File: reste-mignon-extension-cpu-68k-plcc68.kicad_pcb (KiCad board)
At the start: 2 copper layers, 99.1 x 99.1 mm, 20 parts, among them J1 RESTE_MIGNON_CPU_CONNECTOR_A, J2 RESTE_MIGNON_CPU_CONNECTOR_B, U1 MC68000_PLCC_68_PHY

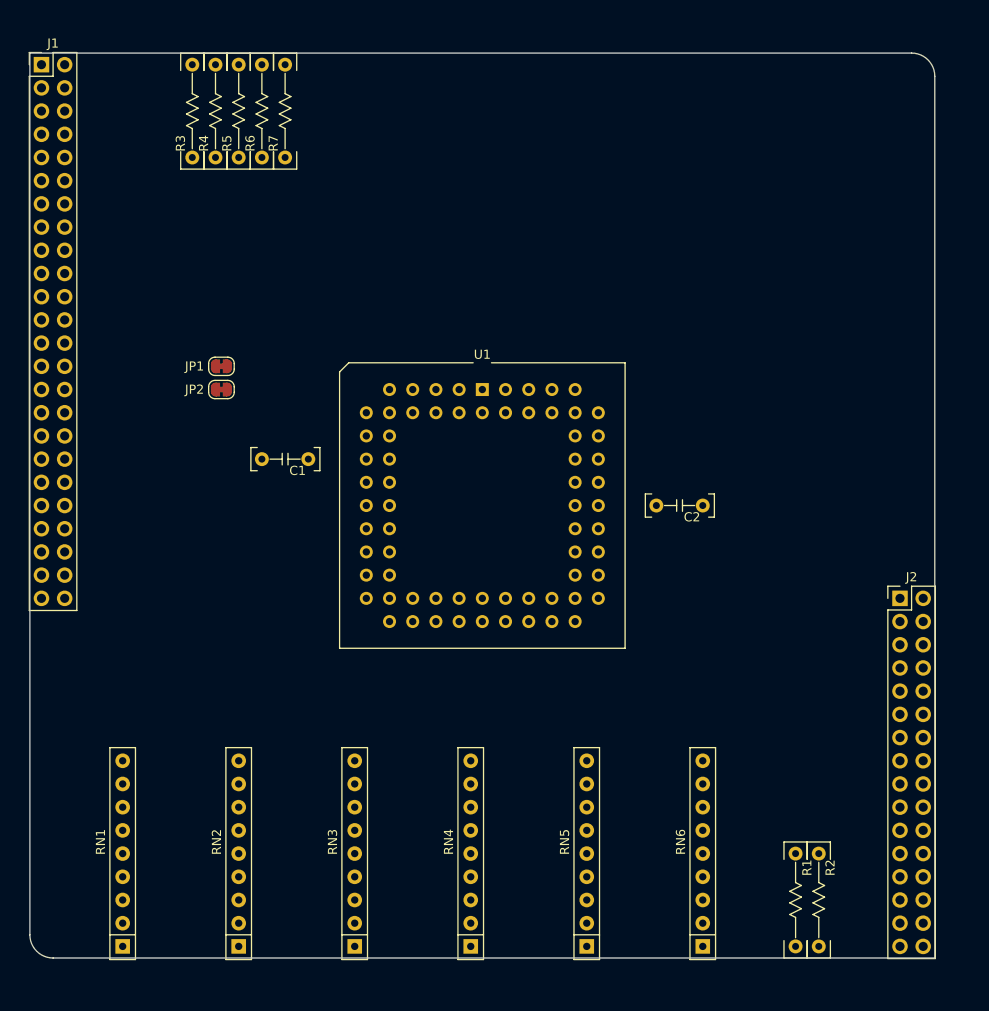
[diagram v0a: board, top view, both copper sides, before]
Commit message: pcb session -- change cpu orientation for easier routing
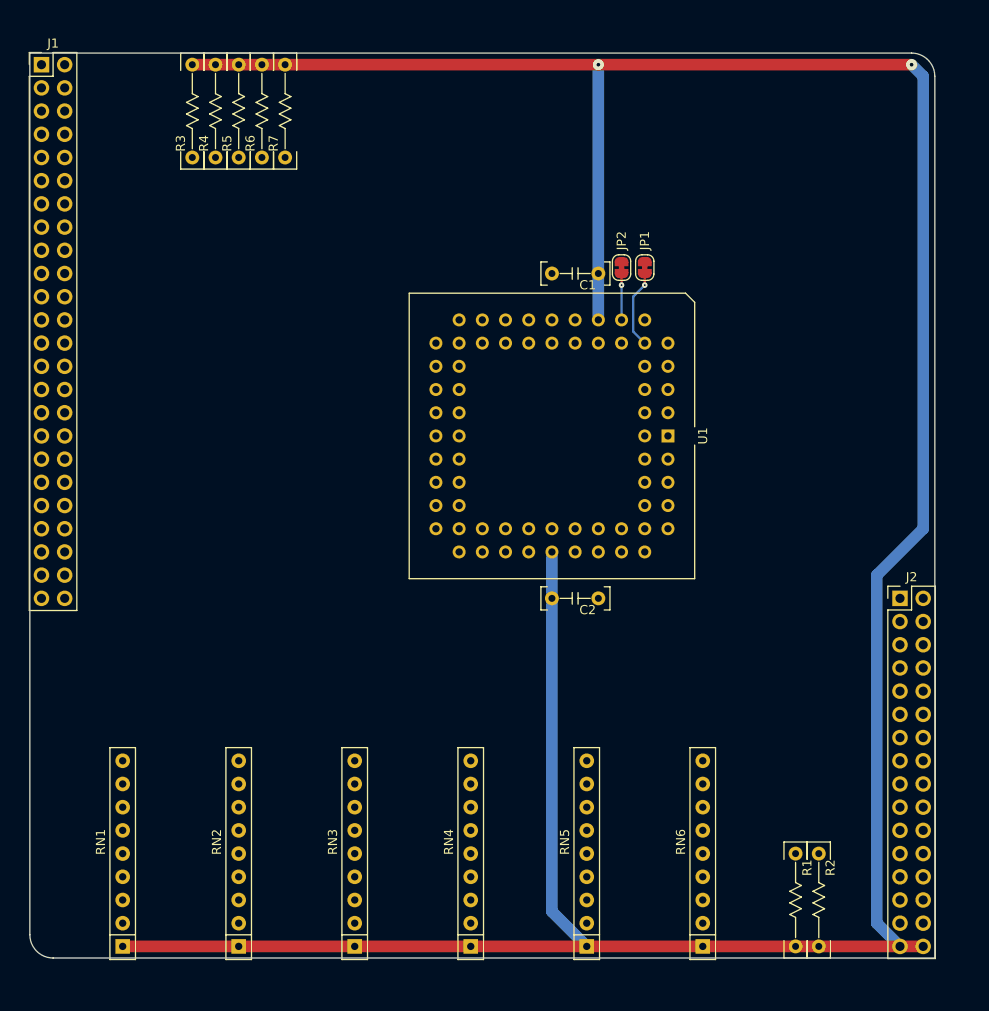
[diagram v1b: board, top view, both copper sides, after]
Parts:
- moved JP1 47.6 mm to (120.7, 125.1), turned to -90 degrees
- moved JP2 45.8 mm to (118.1, 125.1), turned to -90 degrees
- moved C1 37.7 mm to (113.0, 125.7)
- moved U1 20.9 mm to (123.2, 143.5), turned to -90 degrees
- moved C2 15.3 mm to (113.0, 161.3)
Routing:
- net /VCC: track 0.00 -> 339.3 mm, vias 0 -> 2
- net /~{BG}: track 0.00 -> 8.67 mm, vias 0 -> 1
- net /~{BGACK}: track 0.00 -> 5.08 mm, vias 0 -> 1

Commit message: pcb session -- start wiring
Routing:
- net /~{BLT.BG}: track 0.00 -> 79.2 mm, vias 0 -> 2
- net /~{BLT.BGACK}: track 0.00 -> 74.9 mm, vias 0 -> 2
- net /~{VMA}: track 0.00 -> 29.2 mm, vias 0 -> 1
- net /FC0: track 0.00 -> 29.2 mm, vias 0 -> 1
- net /~{VPA}: track 0.00 -> 28.5 mm, vias 0 -> 1
- net /FC1: track 0.00 -> 28.5 mm, vias 0 -> 1
- net /FC2: track 0.00 -> 23.4 mm, vias 0 -> 1
- net /~{DTACK}: track 0.00 -> 16.5 mm, vias 0 -> 1
- net /~{RESET}: track 0.00 -> 11.4 mm, vias 0 -> 1
- net /~{AS}: track 0.00 -> 8.15 mm
- net /R/~{W}: track 0.00 -> 8.15 mm
- net /D8: track 0.00 -> 8.15 mm
- net /D5: track 0.00 -> 8.15 mm
- net /D3: track 0.00 -> 8.15 mm
- net /D15: track 0.00 -> 8.15 mm
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
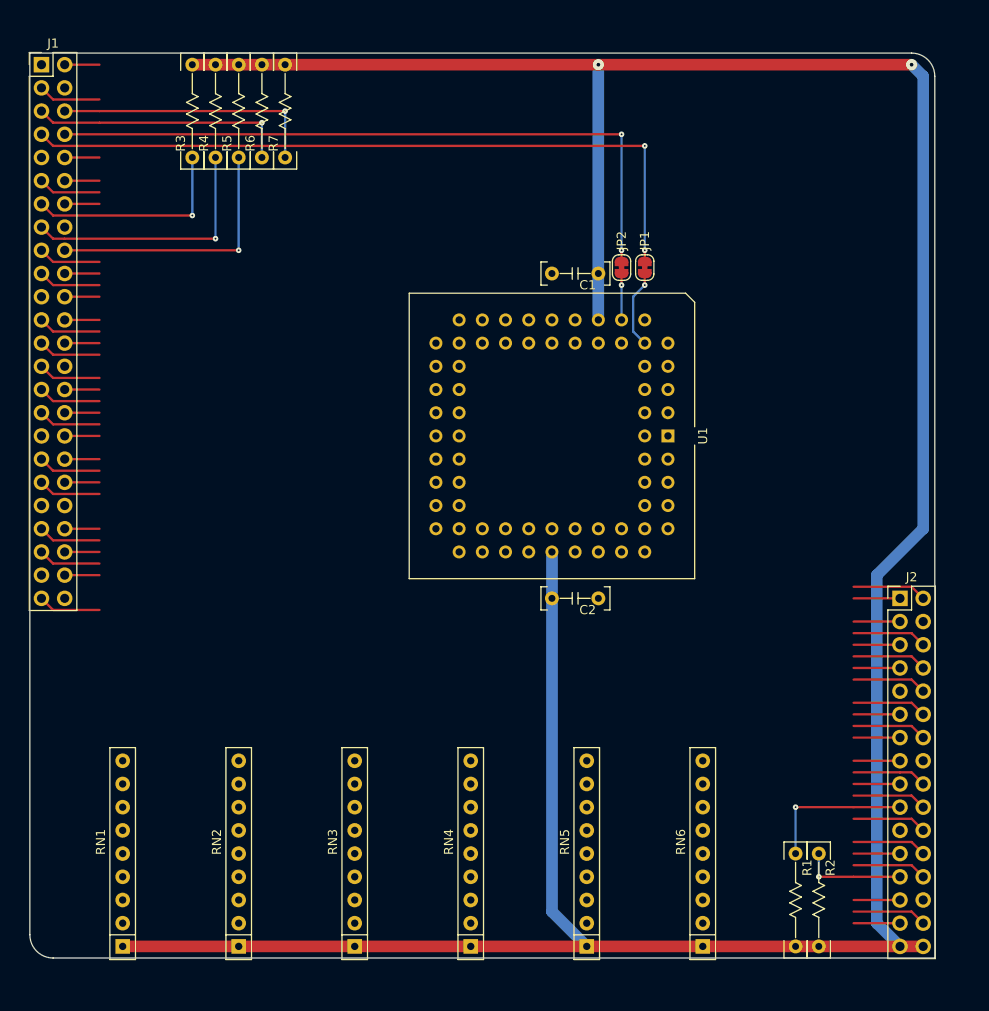
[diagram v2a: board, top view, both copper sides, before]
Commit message: pcb session -- start pull-ups, adjust pull-up mapping of RN1 for ease of routing
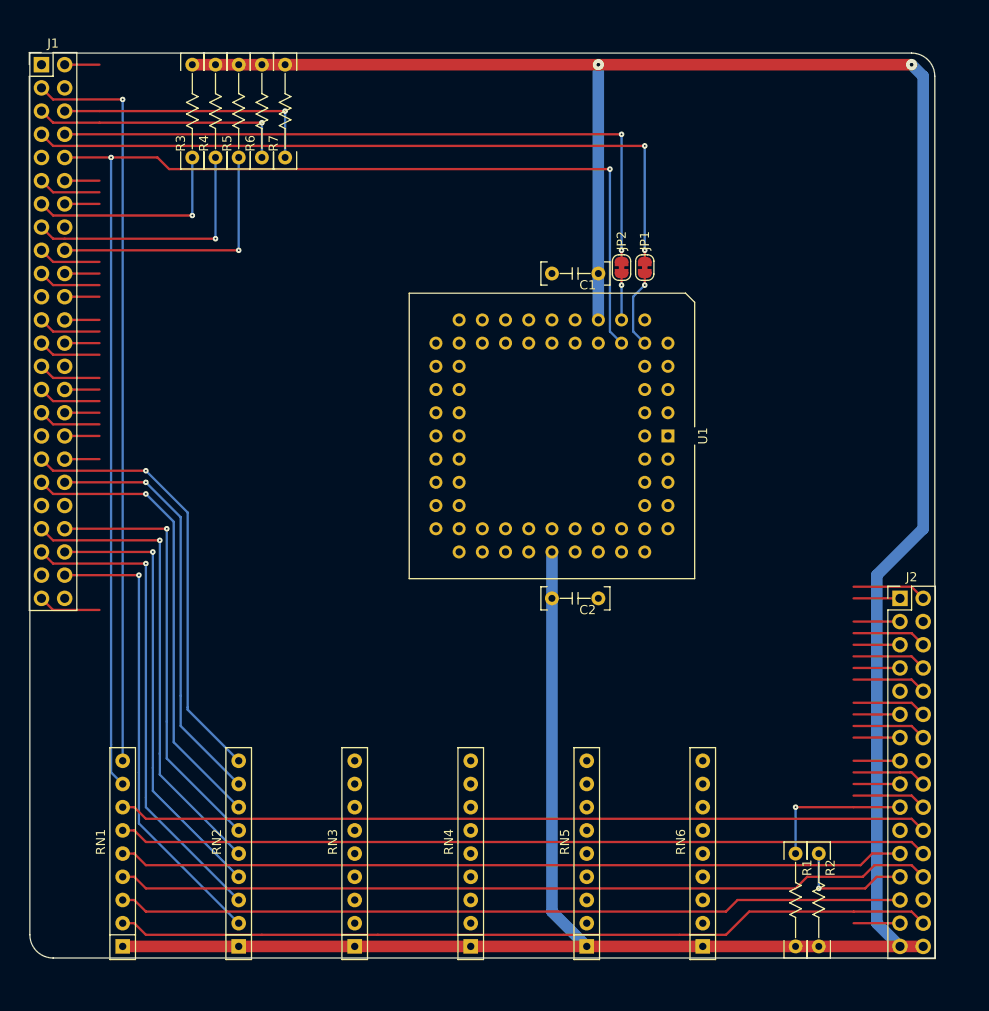
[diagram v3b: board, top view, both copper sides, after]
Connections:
- RN1 pad 2: /~{HALT} -> /~{BGACK}
- RN1 pad 3: /~{BERR} -> /~{HALT}
- RN1 pad 4: /~{BGACK} -> /~{AS}
- RN1 pad 5: /~{BR} -> /~{UDS}
- RN1 pad 6: /R/~{W} -> /~{LDS}
- RN1 pad 7: /~{LDS} -> /R/~{W}
- RN1 pad 8: /~{UDS} -> /~{BR}
- RN1 pad 9: /~{AS} -> /~{BERR}
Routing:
- net /~{BR}: track 3.81 -> 148.9 mm, vias 0 -> 2
- net /~{AS}: track 8.15 -> 89.7 mm
- net /~{BGACK}: track 13.2 -> 94.8 mm
- net /~{UDS}: track 5.08 -> 86.1 mm
- net /~{HALT}: track 5.08 -> 86.1 mm
- net /~{LDS}: track 8.15 -> 88.7 mm
- net /R/~{W}: track 8.15 -> 88.7 mm
- net /~{BERR}: track 6.88 -> 81.8 mm, vias 0 -> 1
- net /A1: track 3.81 -> 50.8 mm, vias 0 -> 1
- net /A2: track 6.88 -> 53.0 mm, vias 0 -> 1
- net /A3: track 3.81 -> 49.1 mm, vias 0 -> 1
- net /A4: track 6.88 -> 51.3 mm, vias 0 -> 1
- net /A5: track 3.81 -> 47.5 mm, vias 0 -> 1
- net /A6: track 6.88 -> 50.5 mm, vias 0 -> 1
- net /A7: track 3.81 -> 46.1 mm, vias 0 -> 1
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
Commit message: pcb session -- continue pull-ups, done a1-a12
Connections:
- RN4 pad 2: /A17 -> /A23
- RN4 pad 3: /A18 -> /A22
- RN4 pad 4: /A19 -> /A21
- RN4 pad 6: /A21 -> /A19
- RN4 pad 7: /A22 -> /A18
- RN4 pad 8: /A23 -> /A17
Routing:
- net /A9: track 3.81 -> 103.8 mm, vias 0 -> 4
- net /A10: track 3.81 -> 97.8 mm, vias 0 -> 4
- net /A11: track 6.88 -> 99.2 mm, vias 0 -> 2
- net /A12: track 3.81 -> 91.2 mm, vias 0 -> 2
- net /A14: track 3.81 -> 67.7 mm, vias 0 -> 1
- net /A16: track 6.88 -> 69.5 mm, vias 0 -> 1
- net /A13: track 6.88 -> 68.9 mm, vias 0 -> 1
- net /A23: track 6.88 -> 68.3 mm, vias 0 -> 2
- net /A15: track 6.88 -> 66.4 mm, vias 0 -> 1
- net /A1: track 50.8 -> 105.4 mm, vias 1 -> 3
- net /A22: track 3.81 -> 57.3 mm, vias 0 -> 2
- net /A21: track 6.88 -> 58.5 mm, vias 0 -> 2
- net /A3: track 49.1 -> 98.6 mm, vias 1 -> 3
- net /A2: track 53.0 -> 102.0 mm, vias 1 -> 3
- net /A5: track 47.5 -> 91.8 mm, vias 1 -> 3
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
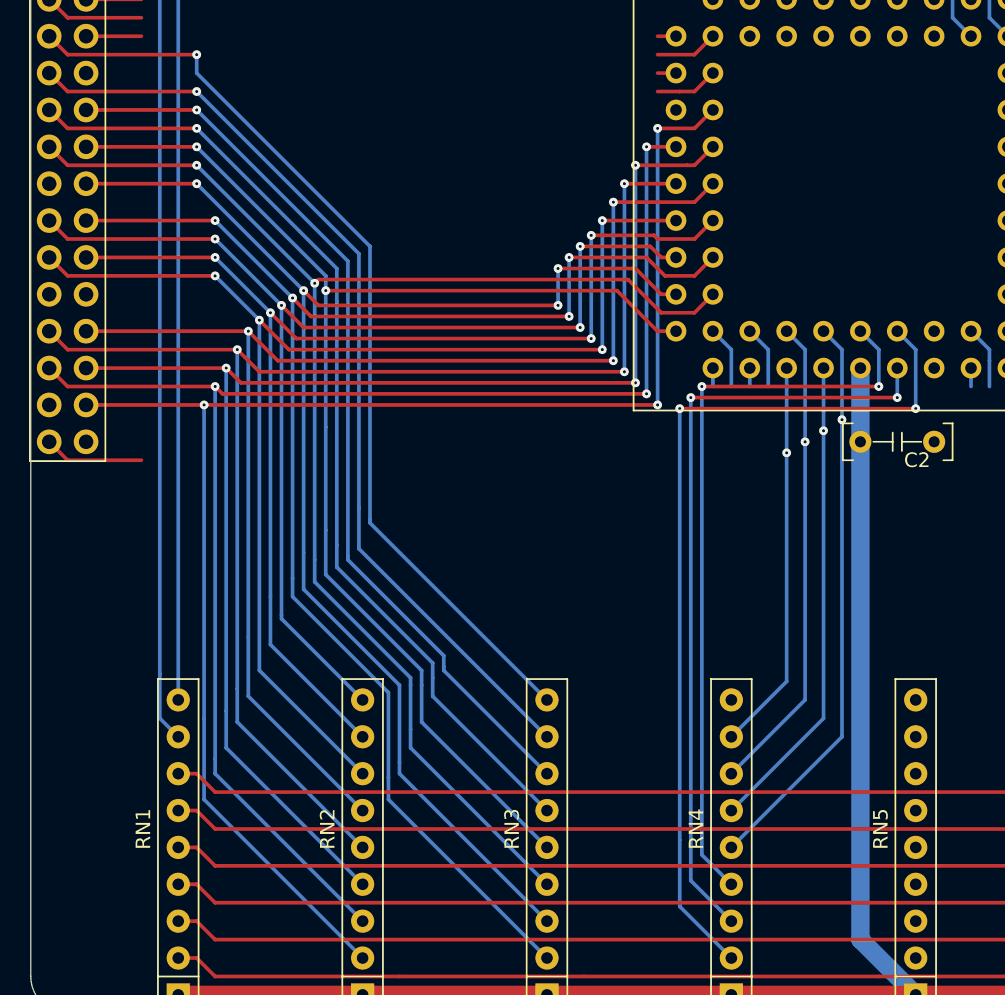
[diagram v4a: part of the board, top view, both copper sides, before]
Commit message: pcb session -- switch to 4 layers, spread vias to avoid cuts in ground plane
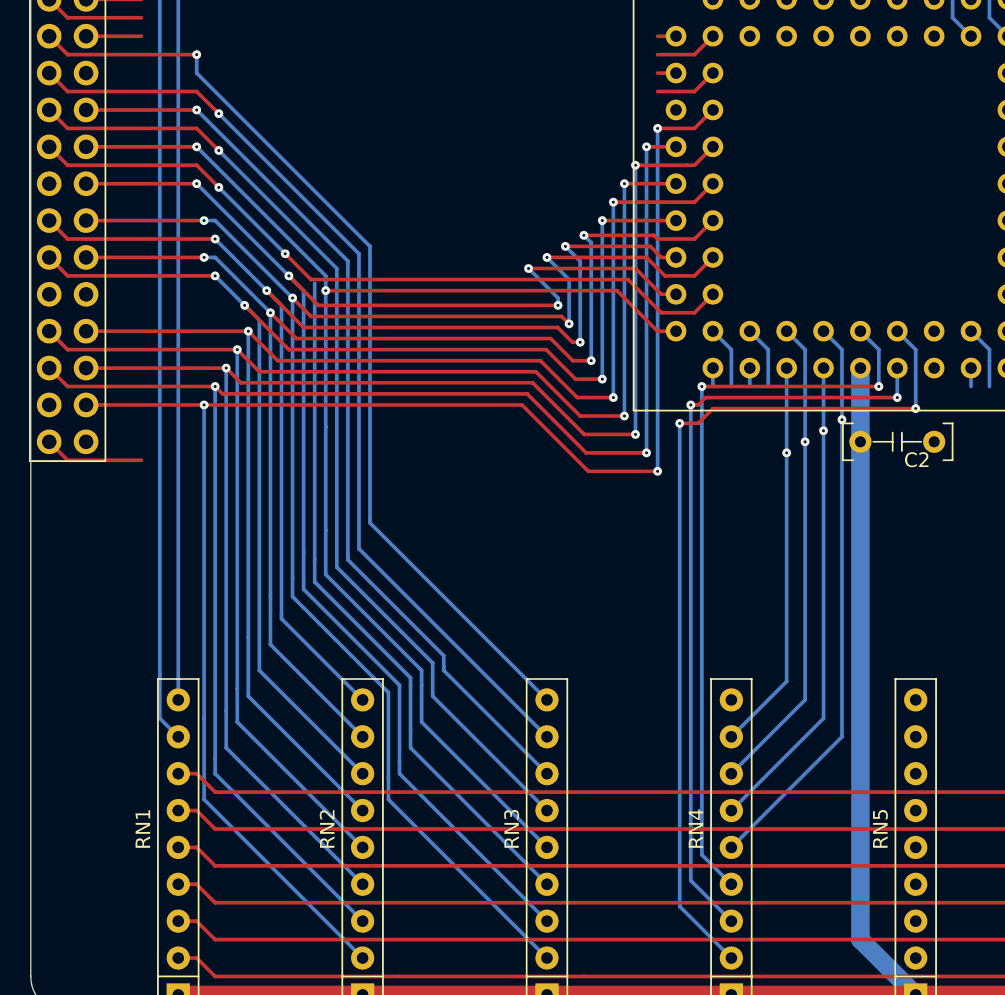
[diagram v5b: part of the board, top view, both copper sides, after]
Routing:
- net /A1: track 105.4 -> 111.8 mm
- net /A2: track 102.0 -> 107.7 mm
- net /A3: track 98.6 -> 103.6 mm
- net /A6: track 88.9 -> 93.2 mm
- net /A4: track 95.2 -> 99.5 mm
- net /A10: track 97.8 -> 102.1 mm
- net /A8: track 81.6 -> 85.9 mm
- net /A5: track 91.8 -> 95.3 mm
- net /A9: track 103.8 -> 106.6 mm
- net /A7: track 85.1 -> 88.0 mm
- net /A23: track 68.3 -> 67.7 mm
- added copper zone on In1.Cu, net /GND
- added copper zone on In2.Cu, net /GND
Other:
- copper layers 2 -> 4

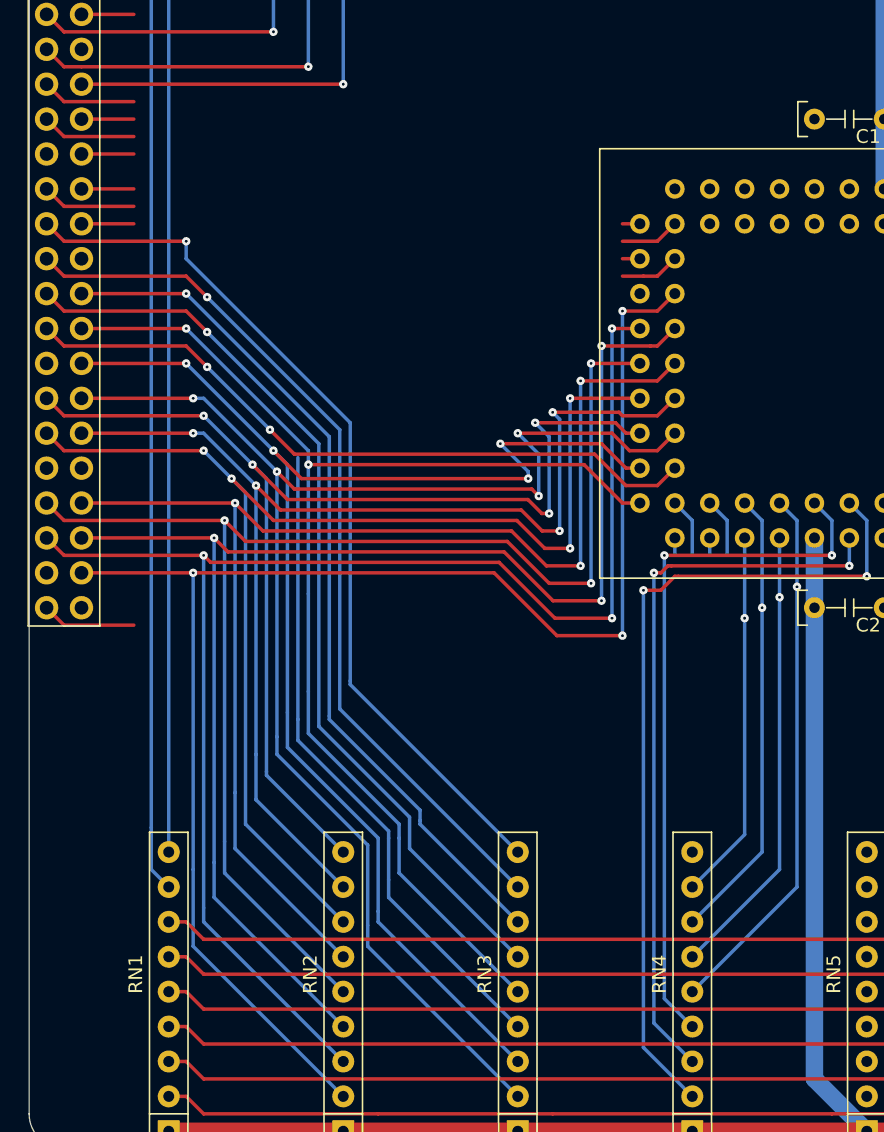
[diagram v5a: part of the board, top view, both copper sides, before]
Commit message: pcb session -- done the address bus a1~a23
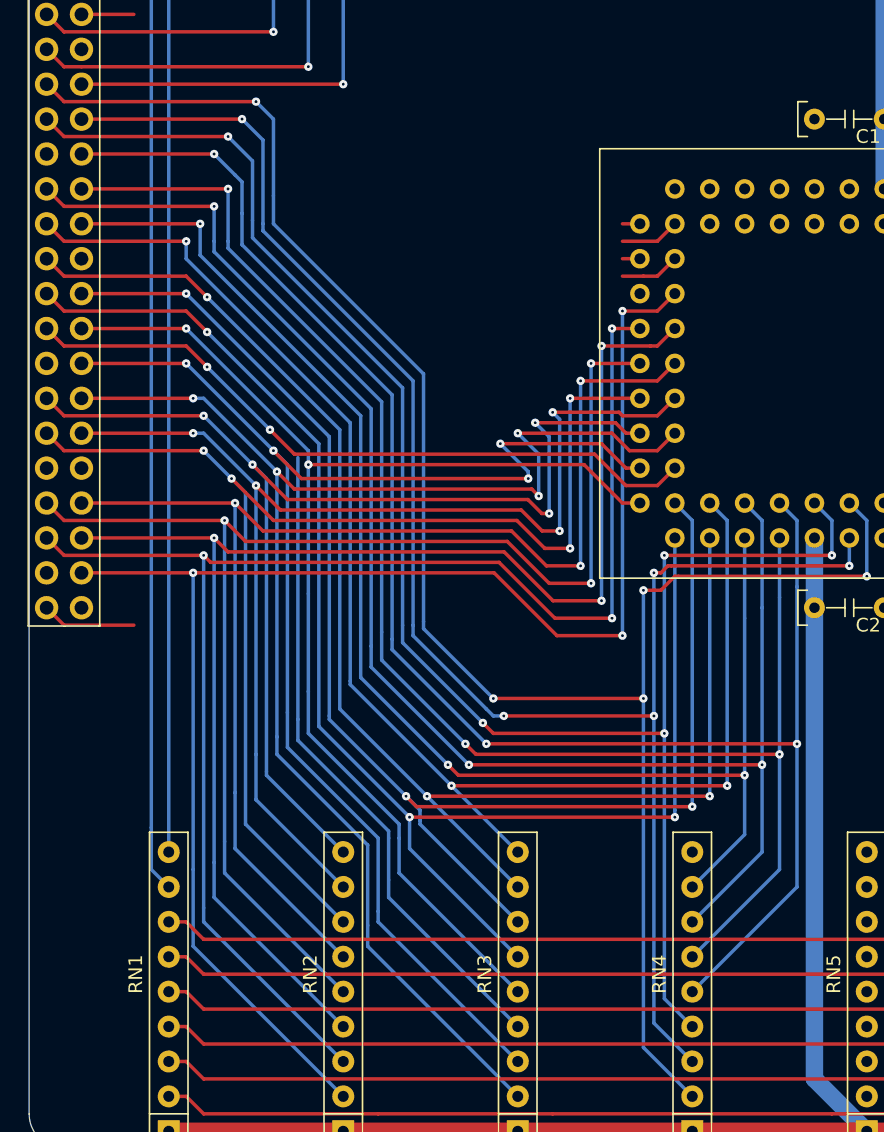
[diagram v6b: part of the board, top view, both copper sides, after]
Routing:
- net /A20: track 43.1 -> 122.6 mm, vias 1 -> 3
- net /A19: track 36.9 -> 114.5 mm, vias 1 -> 3
- net /A18: track 40.0 -> 115.5 mm, vias 1 -> 3
- net /A17: track 30.8 -> 104.4 mm, vias 1 -> 3
- net /A21: track 58.5 -> 129.3 mm, vias 2 -> 5
- net /A22: track 57.0 -> 127.6 mm, vias 2 -> 5
- net /A23: track 67.7 -> 138.1 mm, vias 2 -> 5
- net /A14: track 67.7 -> 107.1 mm, vias 1 -> 3
- net /A13: track 68.9 -> 107.3 mm, vias 1 -> 3
- net /A15: track 66.4 -> 104.5 mm, vias 1 -> 3
- net /A16: track 69.5 -> 106.3 mm, vias 1 -> 3
